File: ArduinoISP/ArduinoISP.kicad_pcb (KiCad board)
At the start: 2 copper layers, 43.2 x 17.8 mm, 15 parts, among them J1 Analog, J2 Digital, J3 AVR-ISP-10, J4 AVR-ISP-6

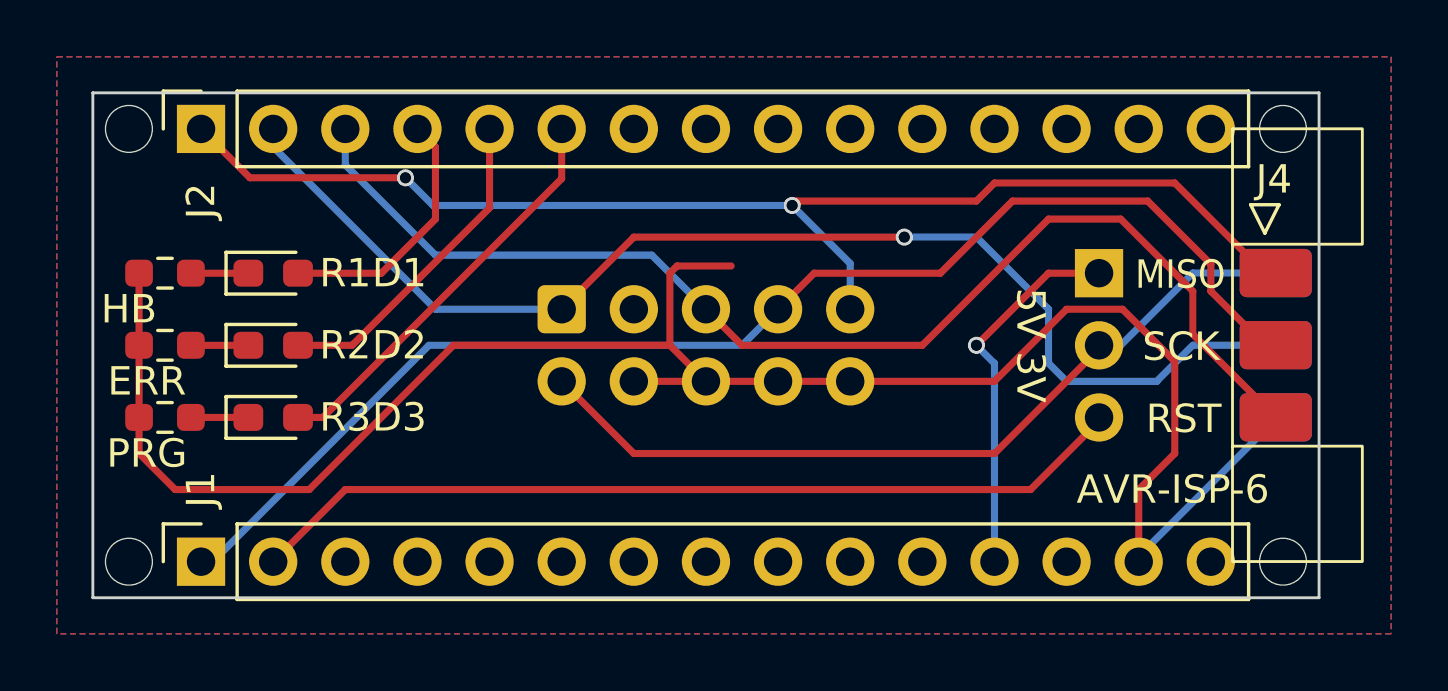
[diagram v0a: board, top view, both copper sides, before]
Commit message: 3d model and gnd fill top right
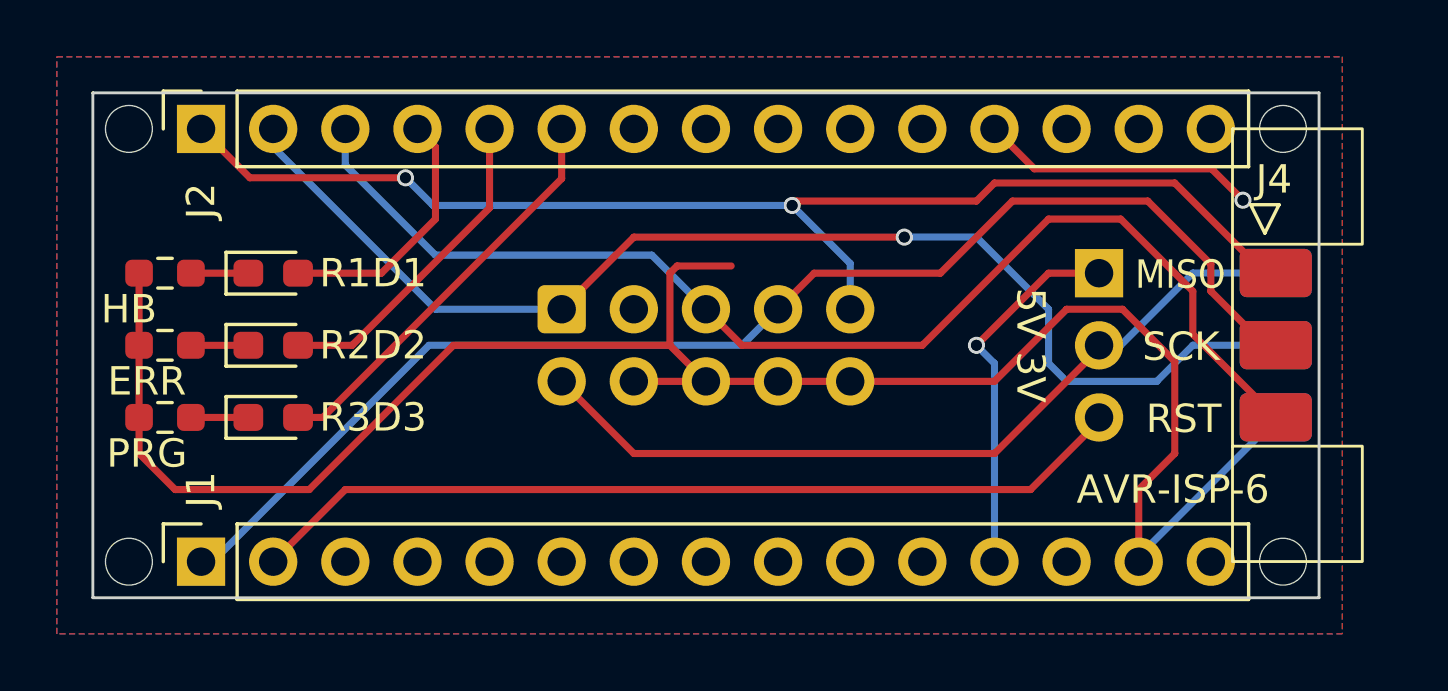
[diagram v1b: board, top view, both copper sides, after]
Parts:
- J4: footprint Arduino_MountingHole:IDC-Header_2x03_P2.54mm_Horizontal -> ArduinoISP:IDC-Header_2x03_P2.54mm_Horizontal
- MH1, MH2, MH3, MH4: footprint Arduino_MountingHole:MountingHole_65mil -> ArduinoISP:MountingHole_65mil
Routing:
- net GND: track 69.8 -> 79.6 mm, vias 0 -> 1
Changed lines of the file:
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@@
 		(legacy_teardrops no)
 	)
-	(paper "A4")
+	(paper "A5")
 	(title_block
-		(date "sam. 04 avril 2015")
+		(title "ArduinoISP")
+		(date "2026-04-11")
+		(company "sD")
 	)
 	(layers
@@
 		)
 	)
-	(footprint "Arduino_MountingHole:MountingHole_65mil"
+	(footprint "ArduinoISP:MountingHole_65mil"
 		(locked yes)
 		(layer "F.Cu")
@@
 		)
 	)
-	(footprint "Arduino_MountingHole:IDC-Header_2x03_P2.54mm_Horizontal"
+	(footprint "ArduinoISP:IDC-Header_2x03_P2.54mm_Horizontal"
 		(layer "F.Cu")
 		(at 141.656 88.565)
@@
 		)
 		(embedded_fonts no)
-		(model "${KICAD10_3DMODEL_DIR}/Connector_IDC.3dshapes/IDC-Header_2x03_P2.54mm_Vertical.step"
+		(model "${KICAD10_3DMODEL_DIR}/Connector_PinSocket_2.54mm.3dshapes/PinSocket_2x03_P2.54mm_Vertical.step"
 			(offset
-				(xyz 2 0 0)
+				(xyz 2 0 -2)
 			)
 			(scale
@@
 		)
 	)
-	(footprint "Arduino_MountingHole:MountingHole_65mil"
+	(footprint "ArduinoISP:MountingHole_65mil"
 		(locked yes)
 		(layer "F.Cu")
@@
 		(embedded_fonts no)
 	)
-	(footprint "Arduino_MountingHole:MountingHole_65mil"
+	(footprint "ArduinoISP:MountingHole_65mil"
 		(locked yes)
 		(layer "F.Cu")
@@
 		)
 	)
-	(footprint "Arduino_MountingHole:MountingHole_65mil"
+	(footprint "ArduinoISP:MountingHole_65mil"
 		(locked yes)
 		(layer "F.Cu")
@@
 	)
 	(gr_text "GND"
-		(at 143.18 96.19 0)
+		(at 143.3 96.19 0)
 		(layer "B.SilkS")
 		(effects
@@
 	)
 	(segment
+		(start 133.155 84.895)
+		(end 139.395 84.895)
+		(width 0.25)
+		(layer "F.Cu")
+		(net "GND")
+	)
+	(segment
+		(start 139.395 84.895)
+		(end 140.5 86)
+		(width 0.25)
+		(layer "F.Cu")
+		(net "GND")
+	)
+	(segment
 		(start 101.6275 94.92)
 		(end 102.8975 96.19)
@@
 	)
 	(segment
+		(start 131.75 83.49)
+		(end 133.155 84.895)
+		(width 0.25)
+		(layer "F.Cu")
+		(net "GND")
+	)
+	(segment
 		(start 120.32 88.57)
 		(end 120.574 88.316)
@@
 		(net "GND")
 	)
+	(via
+		(at 140.5 86)
+		(size 0.6)
+		(drill 0.4)
+		(layers "F.Cu" "B.Cu")
+		(net "GND")
+	)
 	(segment
 		(start 136.83 98.5345)
@@
 		(polygon
 			(pts
-				(xy 98.73 80.95) (xy 145.72 80.95) (xy 145.72 101.27) (xy 98.73 101.27)
+				(xy 98.73 80.95) (xy 144 80.95) (xy 144 101.27) (xy 98.73 101.27)
 			)
 		)
